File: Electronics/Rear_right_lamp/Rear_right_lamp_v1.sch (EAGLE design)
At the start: 11 parts, among them X1 JST-XH-05-PIN-ROUND-PAD

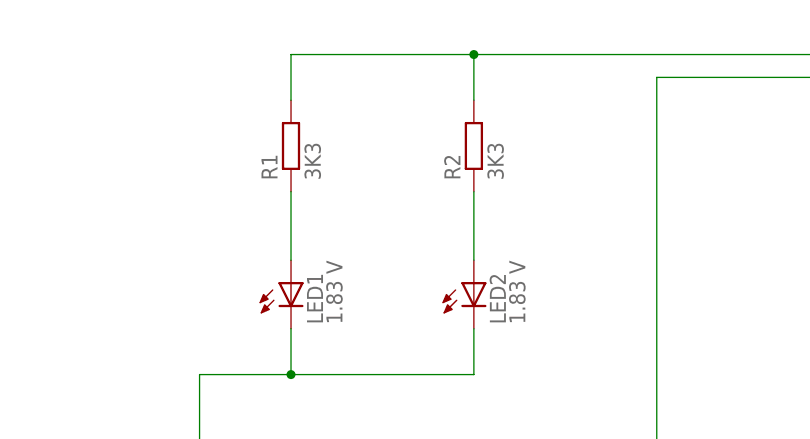
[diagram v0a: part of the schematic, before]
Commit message: Rear lamps improved
Greater resistors' value for API_START_ENGINE
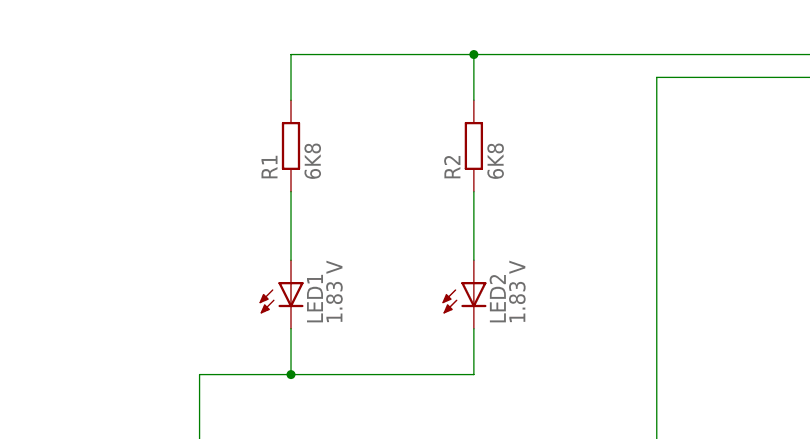
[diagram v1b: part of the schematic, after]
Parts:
- R1, R2: value 3K3 -> 6K8
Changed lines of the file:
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@@
 <attribute name="CURRENT" value="1.42 mA"/>
 </part>
-<part name="R1" library="resistor" deviceset="R-EU_" device="0204/2V" value="3K3"/>
-<part name="R2" library="resistor" deviceset="R-EU_" device="0204/2V" value="3K3"/>
+<part name="R1" library="resistor" deviceset="R-EU_" device="0204/2V" value="6K8"/>
+<part name="R2" library="resistor" deviceset="R-EU_" device="0204/2V" value="6K8"/>
 <part name="R3" library="resistor" deviceset="R-EU_" device="0204/2V" value="680"/>
 <part name="R4" library="resistor" deviceset="R-EU_" device="0204/2V" value="1K"/>
